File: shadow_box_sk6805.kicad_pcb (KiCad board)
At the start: 2 copper layers, 100 x 73 mm, 180 parts, among them J1 USB_B_Micro, U1 ATtiny88-AU, U2 MCP7940N-xST, Y1 7pF CL

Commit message: Add ISP header, wire up everything
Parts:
- added J2: AVR-ISP-6, Connector_PinHeader_2.54mm:PinHeader_2x03_P2.54mm_Vertical_SMD, B.Cu at (97.3, 76.0)
- C4, C5, R1, R6, R7, R8, U1, U2, Y1: moved to F.Cu
- moved J1 89.1 mm to (90.7, 124.2), turned to 90 degrees
- moved R4 49.3 mm to (89.0, 75.1), turned to 90 degrees
- moved R5 29.0 mm to (89.0, 113.6), turned to 270 degrees
- moved R7 12.3 mm to (96.5, 118.8), turned to 0 degrees
- moved R8 12.3 mm to (96.5, 116.3), turned to 0 degrees
- moved R1 11.6 mm to (108.5, 119.3), turned to 180 degrees
- moved R6 11.6 mm to (108.5, 116.8), turned to 180 degrees
- moved C1 10.2 mm to (90.4, 92.8)
- moved R3 10.2 mm to (88.4, 98.0)
- moved C2 10.2 mm to (90.4, 95.9)
- moved R2 10.2 mm to (88.4, 90.7)
- moved S1 10.2 mm to (89.0, 82.8)
- moved S2 10.2 mm to (89.0, 105.8)
- moved C4 6.16 mm to (99.6, 133.3)
- moved BT1 6.07 mm to (172.9, 118.0)
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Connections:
- net Net-(R1-Pad2) renamed RESET
- U1 pad 15: GND -> MOSI
- U1 pad 16: GND -> MISO
- U1 pad 17: GND -> SCK
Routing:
- net +5V: track 0.00 -> 841.2 mm, vias 0 -> 53
- net GND: track 0.00 -> 701.2 mm, vias 0 -> 79
- net Net-(BT1-Pad1): track 0.00 -> 104.2 mm, vias 0 -> 1
- net RESET: track 0.00 -> 51.1 mm, vias 0 -> 3
- net /SK6805_7_segment_S0/DIN: track 0.00 -> 48.7 mm, vias 0 -> 2
- net LEDs: track 0.00 -> 39.4 mm, vias 0 -> 2
- net SCK: track 0.00 -> 37.6 mm, vias 0 -> 3
- net HH: track 0.00 -> 36.8 mm
- net MISO: track 0.00 -> 33.3 mm, vias 0 -> 1
- net MOSI: track 0.00 -> 27.6 mm, vias 0 -> 1
- net /SK6805_7_segment_M1/DIN: track 0.00 -> 26.9 mm, vias 0 -> 2
- net /SK6805_7_segment_M0/DIN: track 0.00 -> 26.7 mm, vias 0 -> 8
- net /SK6805_7_segment_H1/DIN: track 0.00 -> 26.6 mm, vias 0 -> 12
- net MM: track 0.00 -> 26.5 mm
- net /SK6805_7_segment_S1/DIN: track 0.00 -> 26.1 mm, vias 0 -> 2
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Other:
- board text added: "+5V"
- board text added: "GND"
- board text added: "Hour"
- board text added: "MISO"
- board text added: "MOSI"
- board text added: "Minute"
- board text added: "RST"
- board text added: "SCK"
- board text added: "WM v0.0.0 04/13/20"

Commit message: Optimize ground plane a bit; output gbr
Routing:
- net GND: track 701.2 -> 725.4 mm, vias 79 -> 95
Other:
- outline, holes or cut-outs redrawn

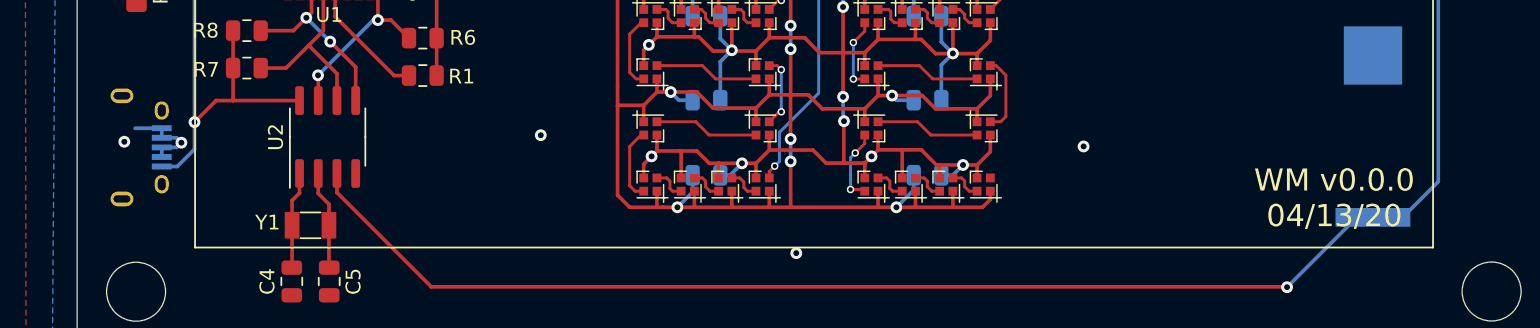
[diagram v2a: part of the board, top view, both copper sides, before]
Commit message: Update usb position, byline
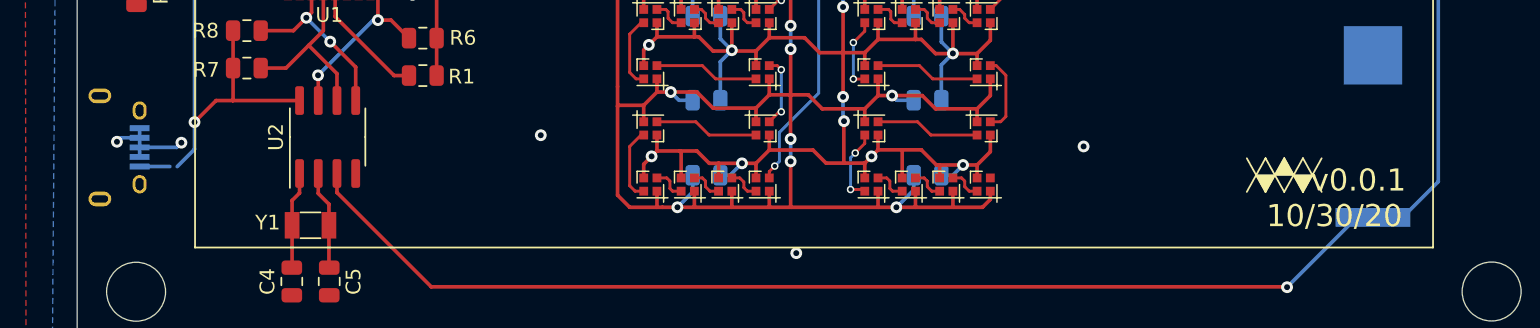
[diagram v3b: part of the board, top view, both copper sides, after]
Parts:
- added REF**: Logo_WM, Symbol:Logo_WM, F.Cu at (166.9, 126.1)
- moved J1 1.50 mm to (89.2, 124.2)
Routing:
- net +5V: track 841.2 -> 842.2 mm
- net GND: track 725.4 -> 725.9 mm
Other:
- board text added: "v0.0.1 10/30/20"
- board text removed: "WM v0.0.0 04/13/20"
